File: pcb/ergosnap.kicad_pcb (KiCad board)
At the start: 2 copper layers, 140 x 135.5 mm, 41 parts, among them J0 Conn_01x05_Female, J1 5PIN, SW1 switch_diode, SW10 switch_diode, SW11 switch_diode, SW12 switch_diode, SW13 switch_diode, SW14 switch_diode, SW15 switch_diode, SW16 switch_diode, SW17 switch_diode, SW18 switch_diode, SW19 switch_diode, SW2 switch_diode, SW20 switch_diode, SW21 switch_diode, SW22 switch_diode, SW23 switch_diode, SW24 switch_diode, SW25 switch_diode, SW26 switch_diode, SW27 switch_diode, SW28 switch_diode, SW3 switch_diode, SW30 switch_diode, SW31 switch_diode, SW32 switch_diode, SW33 switch_diode, SW34 switch_diode, SW35 switch_diode, SW4 switch_diode, SW5 switch_diode, SW6 switch_diode, SW7 switch_diode, SW8 switch_diode, SW9 switch_diode, U3 ProMicro

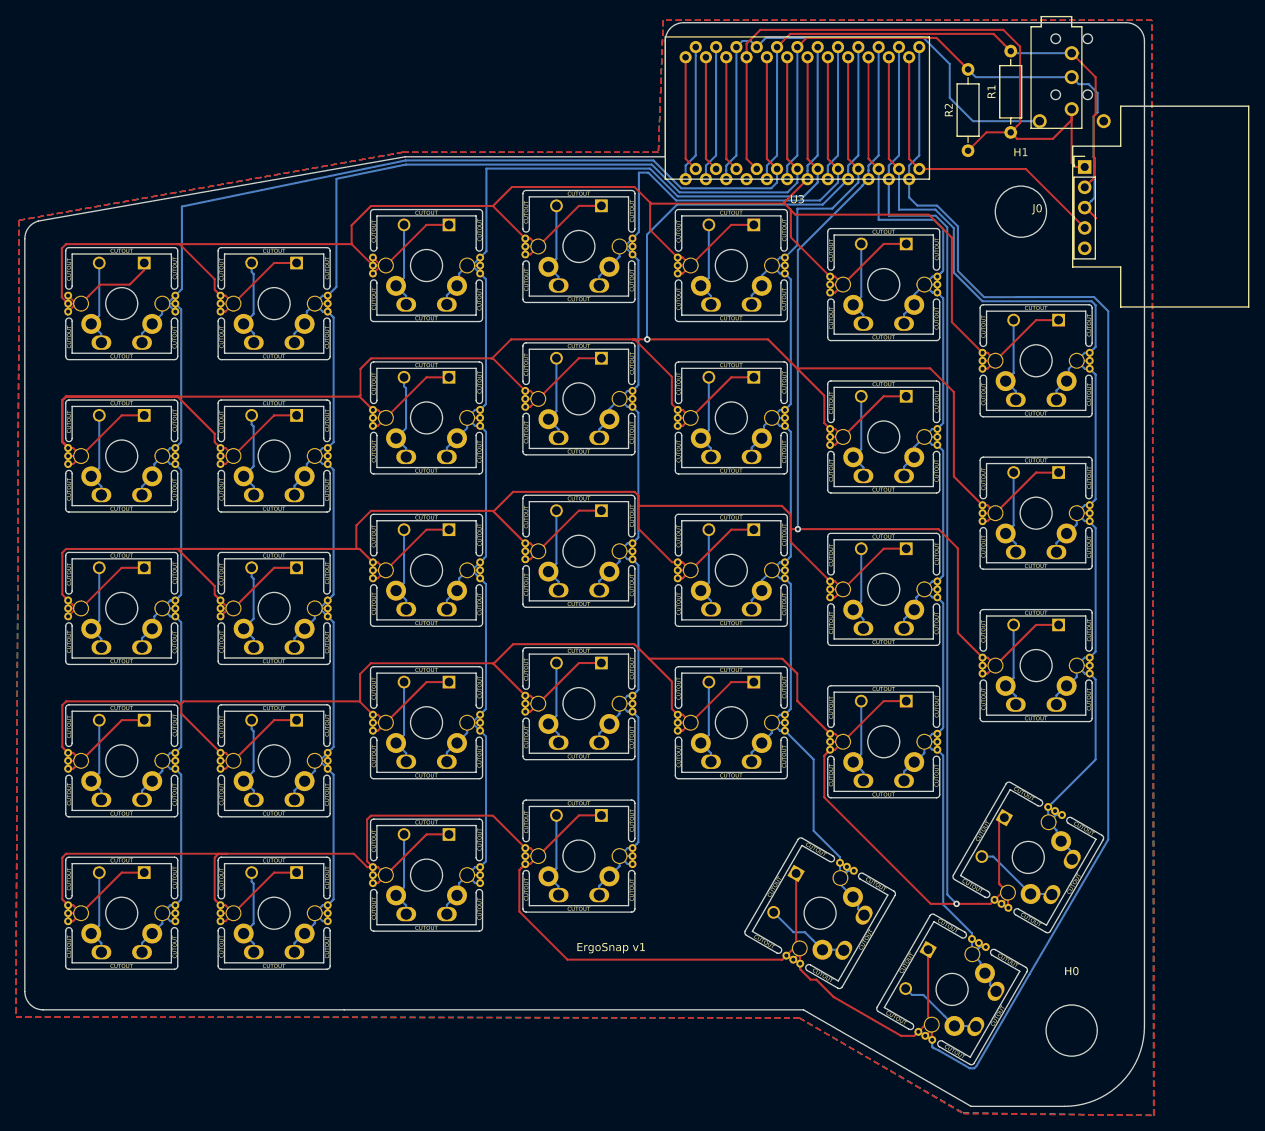
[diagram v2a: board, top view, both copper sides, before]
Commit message: Move diode holes to correct spacing
Incorrectly measured this, diodes don't fit!
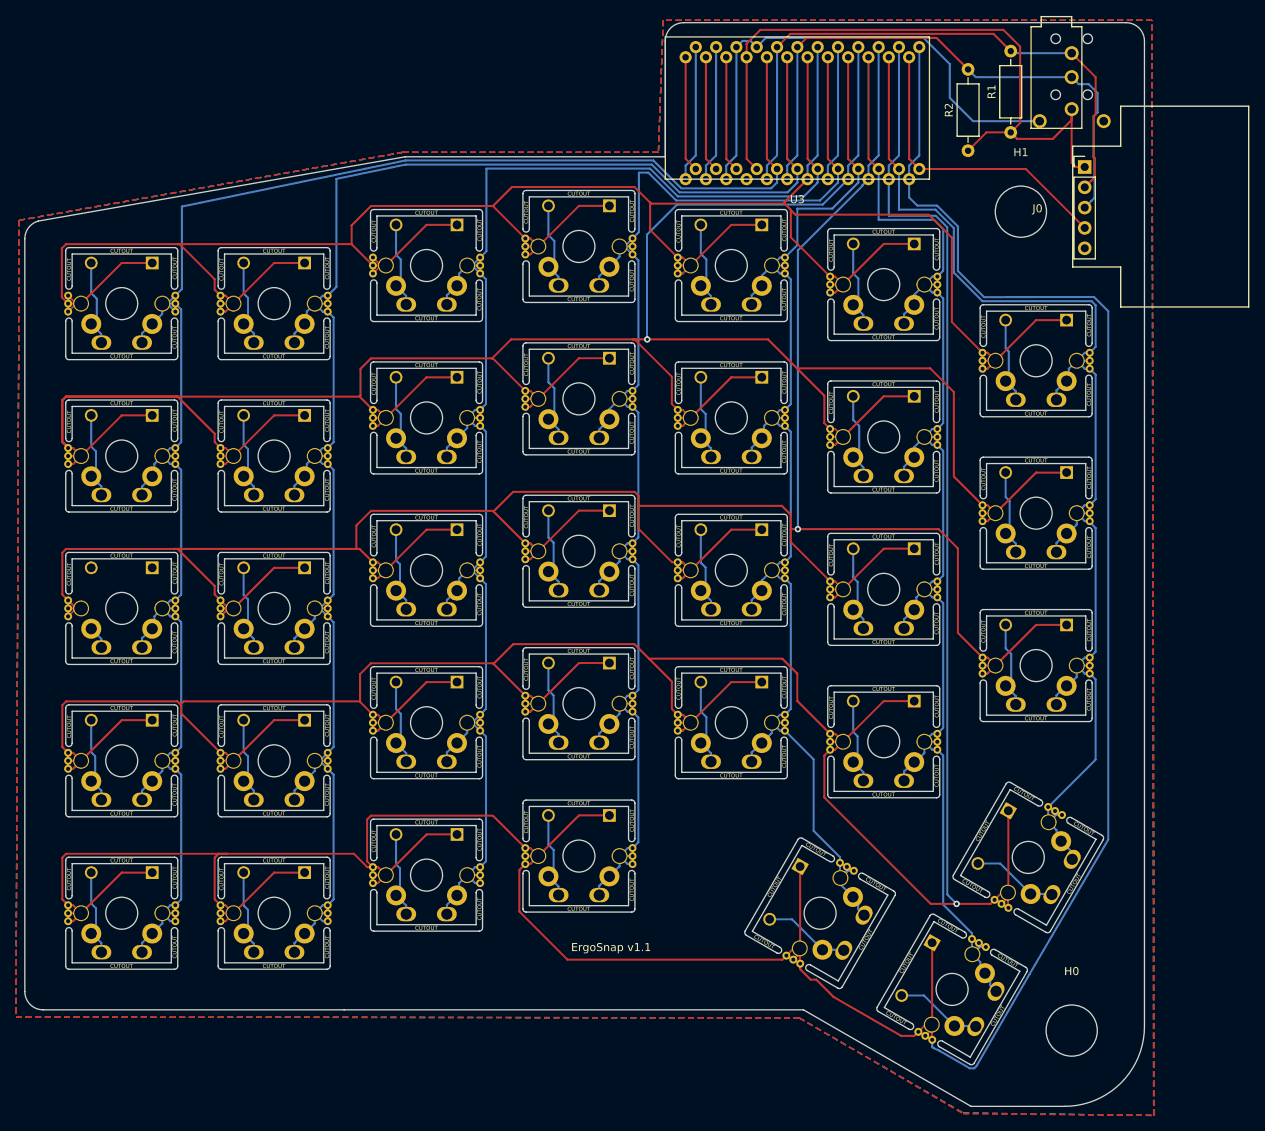
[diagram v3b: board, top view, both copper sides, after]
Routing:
- net Net-(SW3-Pad0): track 10.9 -> 2.86 mm
- net /row1: track 367.2 -> 374.2 mm
- net /row4: track 395.2 -> 401.9 mm
- net /row0: track 308.9 -> 315.4 mm
- net /row3: track 396.7 -> 402.9 mm
- net /row2: track 351.4 -> 347.4 mm
- net /sda: track 75.5 -> 73.6 mm
- net /scl: track 76.5 -> 75.6 mm
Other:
- board text added: "ErgoSnap v1.1"
- board text removed: "ErgoSnap v1"

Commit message: Rev1.1 final (?)
- Added reset header
- Reshaped the bottom of the board slightly
- Moved most of the component references off the silkscreen
- Marked pin 1 in ProMicro footprint
- Added 2 switch traces missed in last update
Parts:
- added J2: Conn_01x02_Female, Connector_Wire:SolderWirePad_1x02_P3.81mm_Drill0.8mm, F.Cu at (213.5, 26.6)
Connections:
- U3 pad 22: Net-(U3-Pad22) -> /rst
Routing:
- net /rst: track 0.00 -> 69.0 mm
- net Net-(U3-Pad22): track 14.5 -> 0.00 mm
- net /row2: track 347.4 -> 358.4 mm
- net Net-(SW3-Pad0): track 2.86 -> 10.9 mm
- net VCC: track 88.3 -> 87.6 mm
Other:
- outline, holes or cut-outs redrawn
- board text added: "RST"
